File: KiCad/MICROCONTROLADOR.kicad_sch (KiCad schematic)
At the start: 13 parts, among them J1 Screw_Terminal_01x05, SW1 SW_Push, U1 PIC24HJ128GP502, Y1 8 MHz

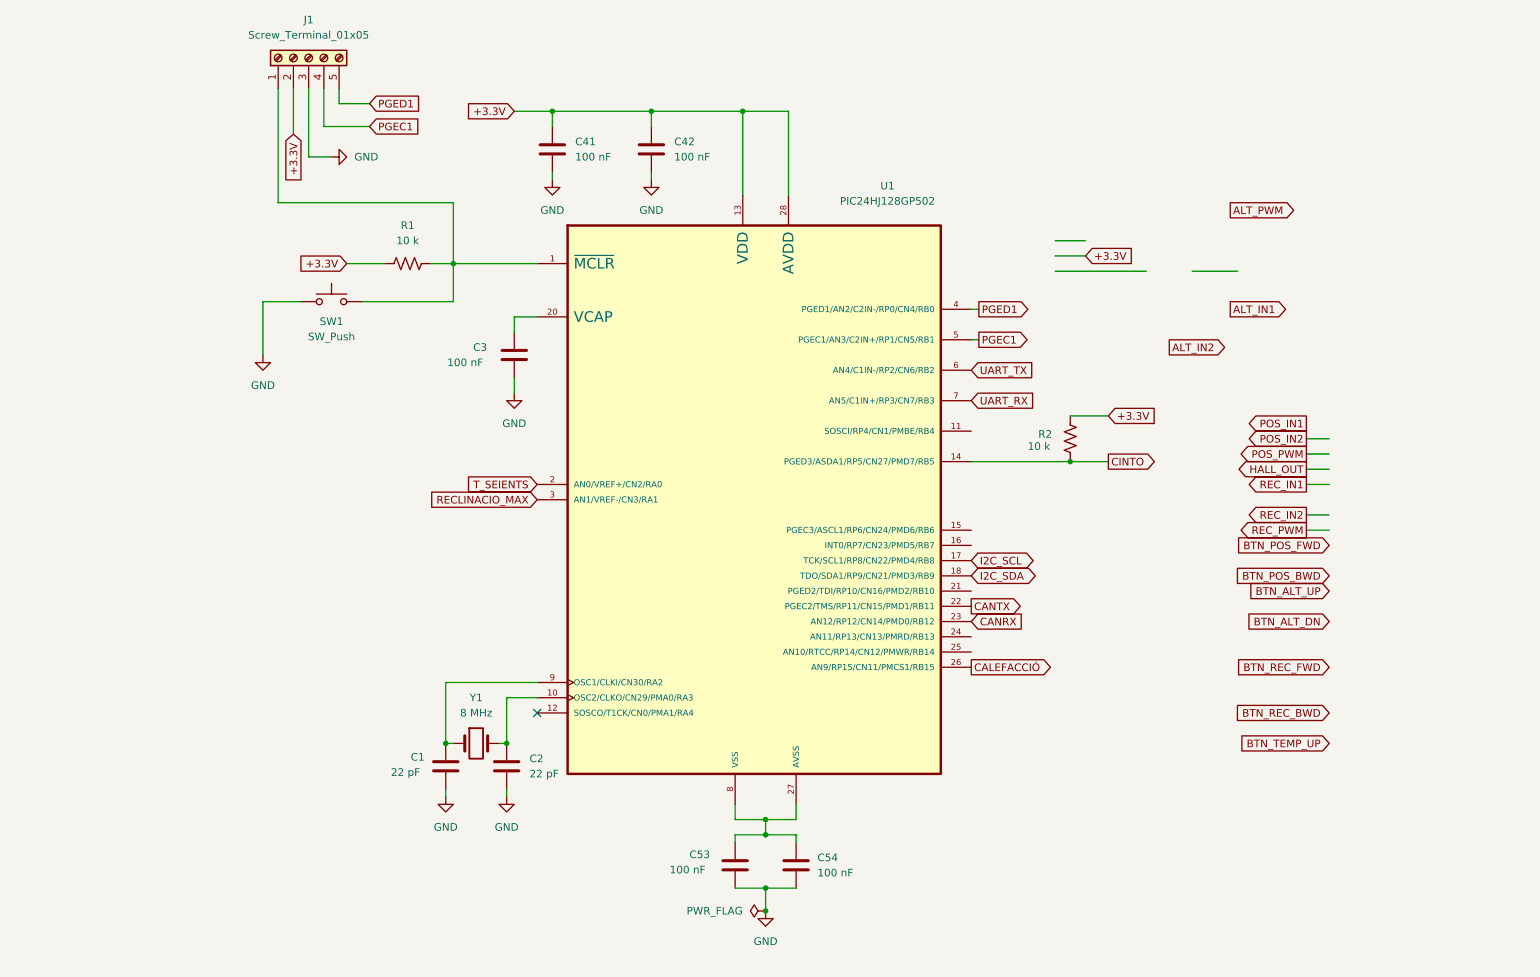
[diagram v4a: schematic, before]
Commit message: canvia al microcontrolador
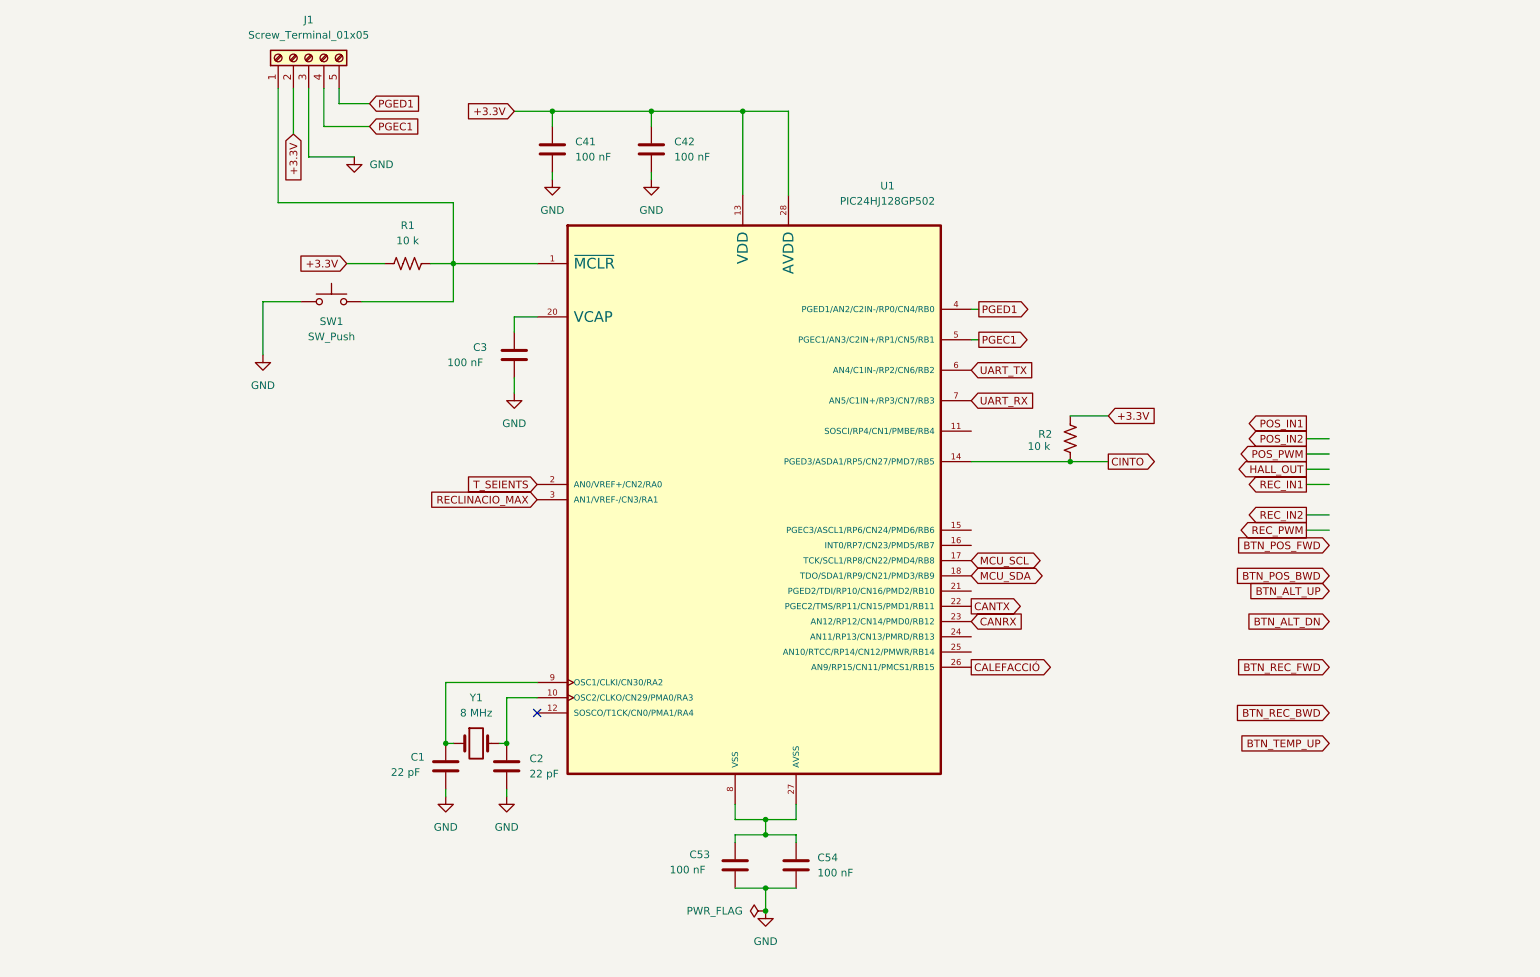
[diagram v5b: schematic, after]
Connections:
- net I2C_SCL renamed MCU_SCL
- net I2C_SDA renamed MCU_SDA
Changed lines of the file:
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@@
-	(wire
-		(pts
-			(xy 194.31 60.96) (xy 209.55 60.96)
-		)
-		(stroke
-			(width 0)
-			(type default)
-		)
-	)
 	(wire
 		(pts
@@
 	(wire
 		(pts
-			(xy 217.17 60.96) (xy 224.79 60.96)
-		)
-		(stroke
-			(width 0)
-			(type default)
-		)
-	)
-	(wire
-		(pts
 			(xy 74.93 33.02) (xy 74.93 30.48)
 		)
@@
 	(wire
 		(pts
-			(xy 73.66 41.91) (xy 69.85 41.91)
+			(xy 77.47 41.91) (xy 69.85 41.91)
 		)
 		(stroke
@@
 	(wire
 		(pts
-			(xy 194.31 58.42) (xy 199.39 58.42)
-		)
-		(stroke
-			(width 0)
-			(type default)
-		)
-	)
-	(wire
-		(pts
 			(xy 180.34 92.71) (xy 196.85 92.71)
 		)
@@
 	(wire
 		(pts
-			(xy 194.31 55.88) (xy 199.39 55.88)
-		)
-		(stroke
-			(width 0)
-			(type default)
-		)
-	)
-	(wire
-		(pts
 			(xy 127 36.83) (xy 127 34.29)
 		)
@@
 			(width 0)
 			(type default)
+		)
+	)
+	(global_label "MCU_SDA"
+		(shape bidirectional)
+		(at 180.34 111.76 0)
+		(fields_autoplaced yes)
+		(effects
+			(font
+				(size 1.27 1.27)
+			)
+			(justify left)
+		)
+		(property "Intersheetrefs" "${INTERSHEET_REFS}"
+			(at 193.0241 111.76 0)
+			(effects
+				(font
+					(size 1.27 1.27)
+				)
+				(justify left)
+				(hide yes)
+			)
 		)
 	)
@@
 		)
 	)
-	(global_label "ALT_PWM"
-		(shape output)
-		(at 223.52 50.8 0)
+	(global_label "BTN_POS_FWD"
+		(shape input)
+		(at 240.03 106.68 180)
+		(fields_autoplaced yes)
+		(effects
+			(font
+				(size 1.27 1.27)
+			)
+			(justify right)
+		)
+		(property "Intersheetrefs" "${INTERSHEET_REFS}"
+			(at 224.5757 106.68 0)
+			(effects
+				(font
+					(size 1.27 1.27)
+				)
+				(justify right)
+				(hide yes)
+			)
+		)
+	)
+	(global_label "UART_RX"
+		(shape input)
+		(at 180.34 82.55 0)
 		(fields_autoplaced yes)
 		(effects
@@
 		)
 		(property "Intersheetrefs" "${INTERSHEET_REFS}"
-			(at 234.0757 50.8 0)
-			(effects
-				(font
-					(size 1.27 1.27)
-				)
-				(justify left)
-				(hide yes)
-			)
-		)
-	)
-	(global_label "BTN_POS_FWD"
-		(shape input)
-		(at 240.03 106.68 180)
-		(fields_autoplaced yes)
-		(effects
-			(font
-				(size 1.27 1.27)
-			)
-			(justify right)
-		)
-		(property "Intersheetrefs" "${INTERSHEET_REFS}"
-			(at 224.5757 106.68 0)
-			(effects
-				(font
-					(size 1.27 1.27)
-				)
-				(justify right)
-				(hide yes)
-			)
-		)
-	)
-	(global_label "UART_RX"
-		(shape input)
-		(at 180.34 82.55 0)
+			(at 191.429 82.55 0)
+			(effects
+				(font
+					(size 1.27 1.27)
+				)
+				(justify left)
+				(hide yes)
+			)
+		)
+	)
+	(global_label "PGED1"
+		(shape input)
+		(at 80.01 33.02 0)
 		(fields_autoplaced yes)
 		(effects
@@
 		)
 		(property "Intersheetrefs" "${INTERSHEET_REFS}"
-			(at 191.429 82.55 0)
-			(effects
-				(font
-					(size 1.27 1.27)
-				)
-				(justify left)
-				(hide yes)
-			)
-		)
-	)
-	(global_label "PGED1"
-		(shape input)
-		(at 80.01 33.02 0)
-		(fields_autoplaced yes)
-		(effects
-			(font
-				(size 1.27 1.27)
-			)
-			(justify left)
-		)
-		(property "Intersheetrefs" "${INTERSHEET_REFS}"
 			(at 89.1637 33.02 0)
 			(effects
@@
 				)
 				(justify right)
-				(hide yes)
-			)
-		)
-	)
-	(global_label "ALT_IN1"
-		(shape output)
-		(at 223.52 67.31 0)
-		(fields_autoplaced yes)
-		(effects
-			(font
-				(size 1.27 1.27)
-			)
-			(justify left)
-		)
-		(property "Intersheetrefs" "${INTERSHEET_REFS}"
-			(at 233.0477 67.31 0)
-			(effects
-				(font
-					(size 1.27 1.27)
-				)
-				(justify left)
-				(hide yes)
-			)
-		)
-	)
-	(global_label "I2C_SDA"
-		(shape bidirectional)
-		(at 180.34 111.76 0)
-		(fields_autoplaced yes)
-		(effects
-			(font
-				(size 1.27 1.27)
-			)
-			(justify left)
-		)
-		(property "Intersheetrefs" "${INTERSHEET_REFS}"
-			(at 192.0565 111.76 0)
-			(effects
-				(font
-					(size 1.27 1.27)
-				)
-				(justify left)
 				(hide yes)
 			)
@@
 		)
 	)
-	(global_label "I2C_SCL"
-		(shape bidirectional)
-		(at 180.34 109.22 0)
-		(fields_autoplaced yes)
-		(effects
-			(font
-				(size 1.27 1.27)
-			)
-			(justify left)
-		)
-		(property "Intersheetrefs" "${INTERSHEET_REFS}"
-			(at 191.996 109.22 0)
-			(effects
-				(font
-					(size 1.27 1.27)
-				)
-				(justify left)
-				(hide yes)
-			)
-		)
-	)
 	(global_label "CANTX"
 		(shape output)
@@
 		)
 	)
-	(global_label "ALT_IN2"
-		(shape output)
-		(at 213.36 73.66 0)
-		(fields_autoplaced yes)
-		(effects
-			(font
-				(size 1.27 1.27)
-			)
-			(justify left)
-		)
-		(property "Intersheetrefs" "${INTERSHEET_REFS}"
-			(at 222.8877 73.66 0)
-			(effects
-				(font
-					(size 1.27 1.27)
-				)
-				(justify left)
-				(hide yes)
-			)
-		)
-	)
 	(global_label "BTN_REC_BWD"
 		(shape input)
@@
 		)
 	)
-	(global_label "+3.3V"
-		(shape input)
-		(at 199.39 58.42 0)
-		(fields_autoplaced yes)
-		(effects
-			(font
-				(size 1.27 1.27)
-			)
-			(justify left)
-		)
-		(property "Intersheetrefs" "${INTERSHEET_REFS}"
-			(at 208.06 58.42 0)
-			(effects
-				(font
-					(size 1.27 1.27)
-				)
-				(justify left)
-				(hide yes)
-			)
-		)
-	)
 	(global_label "T_SEIENTS"
 		(shape input)
@@
 				)
 				(justify right)
+				(hide yes)
+			)
+		)
+	)
+	(global_label "MCU_SCL"
+		(shape bidirectional)
+		(at 180.34 109.22 0)
+		(fields_autoplaced yes)
+		(effects
+			(font
+				(size 1.27 1.27)
+			)
+			(justify left)
+		)
+		(property "Intersheetrefs" "${INTERSHEET_REFS}"
+			(at 192.9636 109.22 0)
+			(effects
+				(font
+					(size 1.27 1.27)
+				)
+				(justify left)
 				(hide yes)
 			)
@@
 	(symbol
 		(lib_id "power:GND")
-		(at 73.66 41.91 90)
+		(at 77.47 41.91 0)
 		(unit 1)
 		(exclude_from_sim no)
@@
 		(fields_autoplaced yes)
 		(property "Reference" "#PWR05"
-			(at 80.01 41.91 0)
+			(at 77.47 48.26 0)
 			(effects
 				(font
@@
 		)
 		(property "Value" "GND"
-			(at 77.47 41.9099 90)
-			(effects
-				(font
-					(size 1.27 1.27)
-				)
-				(justify right)
+			(at 80.01 43.1799 0)
+			(effects
+				(font
+					(size 1.27 1.27)
+				)
+				(justify left)
 			)
 		)
 		(property "Footprint" ""
-			(at 73.66 41.91 0)
+			(at 77.47 41.91 0)
 			(effects
 				(font
@@
 		)
 		(property "Datasheet" ""
-			(at 73.66 41.91 0)
+			(at 77.47 41.91 0)
 			(effects
 				(font
@@
 		)
 		(property "Description" "Power symbol creates a global label with name \"GND\" , ground"
-			(at 73.66 41.91 0)
-			(effects
-				(font
+			(at 77.47 41.91 0)
+			(effects
+				(font

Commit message: Modificacions Micro
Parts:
- added C9: 100 nF, symbol Device:C
- added R1: 10 k, symbol Device:R_US
- added R23, R24: 4.7k, symbol Device:R_US
- added U7: MCP23017_SP, Package_DIP:DIP-28_W7.62mm, symbol Interface_Expansion:MCP23017_SP
- renumbered C1 to C11, C2 to C14, C3 to C15, C41 to C16, C42 to C17, C53 to C23, C54 to C24, J1 to J3, R1 to R13, R2 to R14, SW1 to SW8, U1 to U8
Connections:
- net +3.3V: now also C9.2, R1.2, R23.2, R24.1, U7.9 (VDD)
- net BTN_ALT_DN: now also U7.4 (GPB3)
- net BTN_ALT_UP: now also U7.5 (GPB4)
- net BTN_POS_BWD: now also U7.6 (GPB5)
- net BTN_POS_FWD: now also U7.7 (GPB6)
- net BTN_REC_BWD: now also U7.2 (GPB1)
- net BTN_REC_FWD: now also U7.3 (GPB2)
- net BTN_TEMP_UP: now also U7.1 (GPB0)
- net GND: now also C9.1, U7.10 (VSS), U7.15 (A0), U7.16 (A1), U7.17 (A2)
- net HALL_OUT: now also U8.11 (SOSCI/RP4/CN1/PMBE/RB4)
- net MCU_SCL: now also R24.2, U7.12 (SCK)
- net MCU_SDA: now also R23.1, U7.13 (SDA)
- net POS_IN1: now also U8.24 (AN11/RP13/CN13/PMRD/RB13)
- net POS_IN2: now also U8.25 (AN10/RTCC/RP14/CN12/PMWR/RB14)
- net POS_PWM: now also U8.21 (PGED2/TDI/RP10/CN16/PMD2/RB10)
- net REC_IN1: now also U8.15 (PGEC3/ASCL1/RP6/CN24/PMD6/RB6)
- net REC_IN2: now also U8.16 (INT0/RP7/CN23/PMD5/RB7)
- net REC_PWM: now also U7.8 (GPB7)
- removed net VSS: U8.19 (VSS)
- new net: R1.1, U7.18 (~{RESET})
- no-connect marks 1 -> 11
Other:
- moved on the sheet: C11, C14, C15, C16, C17, C23, C24, J3, R13, R14, SW8, U8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

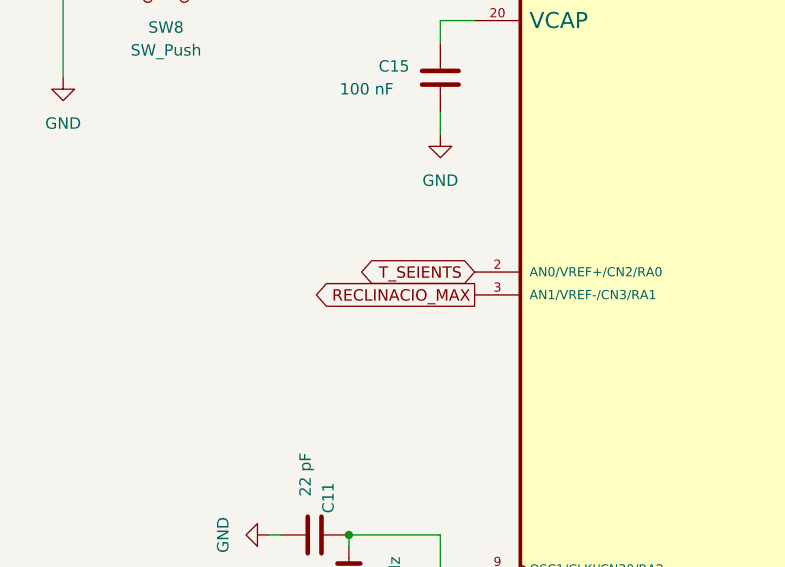
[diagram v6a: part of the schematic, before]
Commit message: Començat el LAYOUT
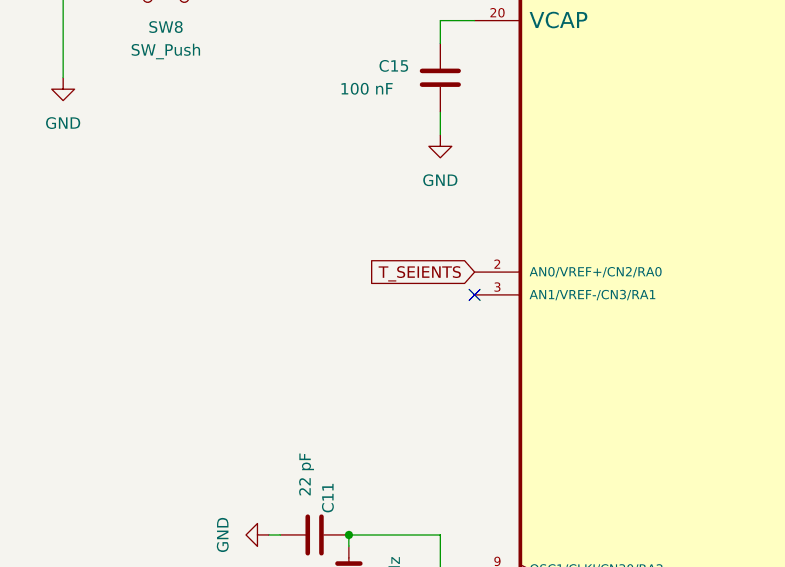
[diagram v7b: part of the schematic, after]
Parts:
- C15: footprint (none) -> Capacitor_THT:CP_Radial_D5.0mm_P2.00mm
- C16, C17: footprint (none) -> Capacitor_THT:C_Disc_D3.0mm_W1.6mm_P2.50mm
- R1, R13, R14, R23, R24: footprint (none) -> Resistor_SMD:R_0805_2012Metric
- SW8: footprint (none) -> Button_Switch_SMD:SW_Push_SPST_NO_Alps_SKRK
- Y1: footprint (none) -> Crystal:Crystal_HC49-4H_Vertical
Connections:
- net RECLINACIO_MAX: no longer names the net of U8.3 (AN1/VREF-/CN3/RA1)
- no-connect marks 11 -> 12
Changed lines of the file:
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@@
 	)
 	(no_connect
+		(at 71.12 101.6)
+	)
+	(no_connect
 		(at 255.27 85.09)
 	)
@@
 		)
 	)
-	(global_label "RECLINACIO_MAX"
-		(shape output)
-		(at 71.12 101.6 180)
-		(fields_autoplaced yes)
-		(effects
-			(font
-				(size 1.27 1.27)
-			)
-			(justify right)
-		)
-		(property "Intersheetrefs" "${INTERSHEET_REFS}"
-			(at 53.1256 101.6 0)
-			(effects
-				(font
-					(size 1.27 1.27)
-				)
-				(justify right)
-				(hide yes)
-			)
-		)
-	)
 	(global_label "REC_IN2"
 		(shape output)
@@
 	)
 	(global_label "T_SEIENTS"
-		(shape bidirectional)
+		(shape input)
 		(at 71.12 99.06 180)
 		(fields_autoplaced yes)
@@
 		)
 		(property "Intersheetrefs" "${INTERSHEET_REFS}"
-			(at 58.2814 99.06 0)
+			(at 59.2339 99.06 0)
 			(effects
 				(font
@@
 			)
 		)
-		(property "Footprint" ""
+		(property "Footprint" "Resistor_SMD:R_0805_2012Metric"
 			(at 49.784 61.214 90)
 			(effects
@@
 			)
 		)
-		(property "Footprint" ""
+		(property "Footprint" "Capacitor_THT:C_Disc_D3.0mm_W1.6mm_P2.50mm"
 			(at 74.6252 46.99 0)
 			(effects
@@
 			)
 		)
-		(property "Footprint" ""
+		(property "Footprint" "Resistor_SMD:R_0805_2012Metric"
 			(at 213.614 40.386 90)
 			(effects
@@
 			)
 		)
-		(property "Footprint" ""
+		(property "Footprint" "Resistor_SMD:R_0805_2012Metric"
 			(at 214.884 50.546 90)
 			(effects
@@
 			)
 		)
-		(property "Footprint" ""
+		(property "Footprint" "Resistor_SMD:R_0805_2012Metric"
 			(at 161.544 91.186 90)
 			(effects
@@
 			)
 		)
-		(property "Footprint" ""
+		(property "Footprint" "Resistor_SMD:R_0805_2012Metric"
 			(at 211.836 68.326 90)
 			(effects
@@
 			)
 		)
-		(property "Footprint" ""
+		(property "Footprint" "Capacitor_THT:CP_Radial_D5.0mm_P2.00mm"
 			(at 68.2752 81.28 0)
 			(effects
@@
 			)
 		)
-		(property "Footprint" ""
+		(property "Footprint" "Crystal:Crystal_HC49-4H_Vertical"
 			(at 57.15 133.35 0)
 			(effects
@@
 			)
 		)
-		(property "Footprint" ""
+		(property "Footprint" "Button_Switch_SMD:SW_Push_SPST_NO_Alps_SKRK"
 			(at 36.83 63.5 0)
 			(effects
@@
 			)
 		)
-		(property "Footprint" ""
+		(property "Footprint" "Capacitor_THT:C_Disc_D3.0mm_W1.6mm_P2.50mm"
 			(at 91.1352 46.99 0)
 			(effects

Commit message: footprints asignados
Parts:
- C11, C14, C23, C24, C9: footprint (none) -> Capacitor_SMD:C_0805_2012Metric
- C15: footprint Capacitor_THT:CP_Radial_D5.0mm_P2.00mm -> Capacitor_THT:C_Disc_D5.0mm_W2.5mm_P5.00mm
- C16: footprint Capacitor_THT:C_Disc_D3.0mm_W1.6mm_P2.50mm -> Capacitor_THT:C_Disc_D5.0mm_W2.5mm_P5.00mm
- J3: footprint (none) -> TerminalBlock_Phoenix:TerminalBlock_Phoenix_MKDS-1,5-5-5.08_1x05_P5.08mm_Horizontal
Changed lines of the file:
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@@
 			)
 		)
-		(property "Footprint" ""
+		(property "Footprint" "TerminalBlock_Phoenix:TerminalBlock_Phoenix_MKDS-1,5-5-5.08_1x05_P5.08mm_Horizontal"
 			(at 33.02 27.94 0)
 			(effects
@@
 			)
 		)
-		(property "Footprint" ""
+		(property "Footprint" "Capacitor_SMD:C_0805_2012Metric"
 			(at 49.53 139.3952 0)
 			(effects
@@
 			)
 		)
-		(property "Footprint" ""
+		(property "Footprint" "Capacitor_SMD:C_0805_2012Metric"
 			(at 237.49 33.3248 0)
 			(effects
@@
 			)
 		)
-		(property "Footprint" ""
+		(property "Footprint" "Capacitor_SMD:C_0805_2012Metric"
 			(at 115.2652 166.37 0)
 			(effects
@@
 			)
 		)
-		(property "Footprint" "Capacitor_THT:C_Disc_D3.0mm_W1.6mm_P2.50mm"
+		(property "Footprint" "Capacitor_THT:C_Disc_D5.0mm_W2.5mm_P5.00mm"
 			(at 74.6252 46.99 0)
 			(effects
@@
 			)
 		)
-		(property "Footprint" ""
+		(property "Footprint" "Capacitor_SMD:C_0805_2012Metric"
 			(at 105.1052 166.37 0)
 			(effects
@@
 			)
 		)
-		(property "Footprint" "Capacitor_THT:CP_Radial_D5.0mm_P2.00mm"
+		(property "Footprint" "Capacitor_THT:C_Disc_D5.0mm_W2.5mm_P5.00mm"
 			(at 68.2752 81.28 0)
 			(effects
@@
 			)
 		)
-		(property "Footprint" ""
+		(property "Footprint" "Capacitor_SMD:C_0805_2012Metric"
 			(at 49.53 129.2352 0)
 			(effects
